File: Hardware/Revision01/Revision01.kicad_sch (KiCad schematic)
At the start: 21 parts, among them J1 Battery connector, SW1 Power-switch connection

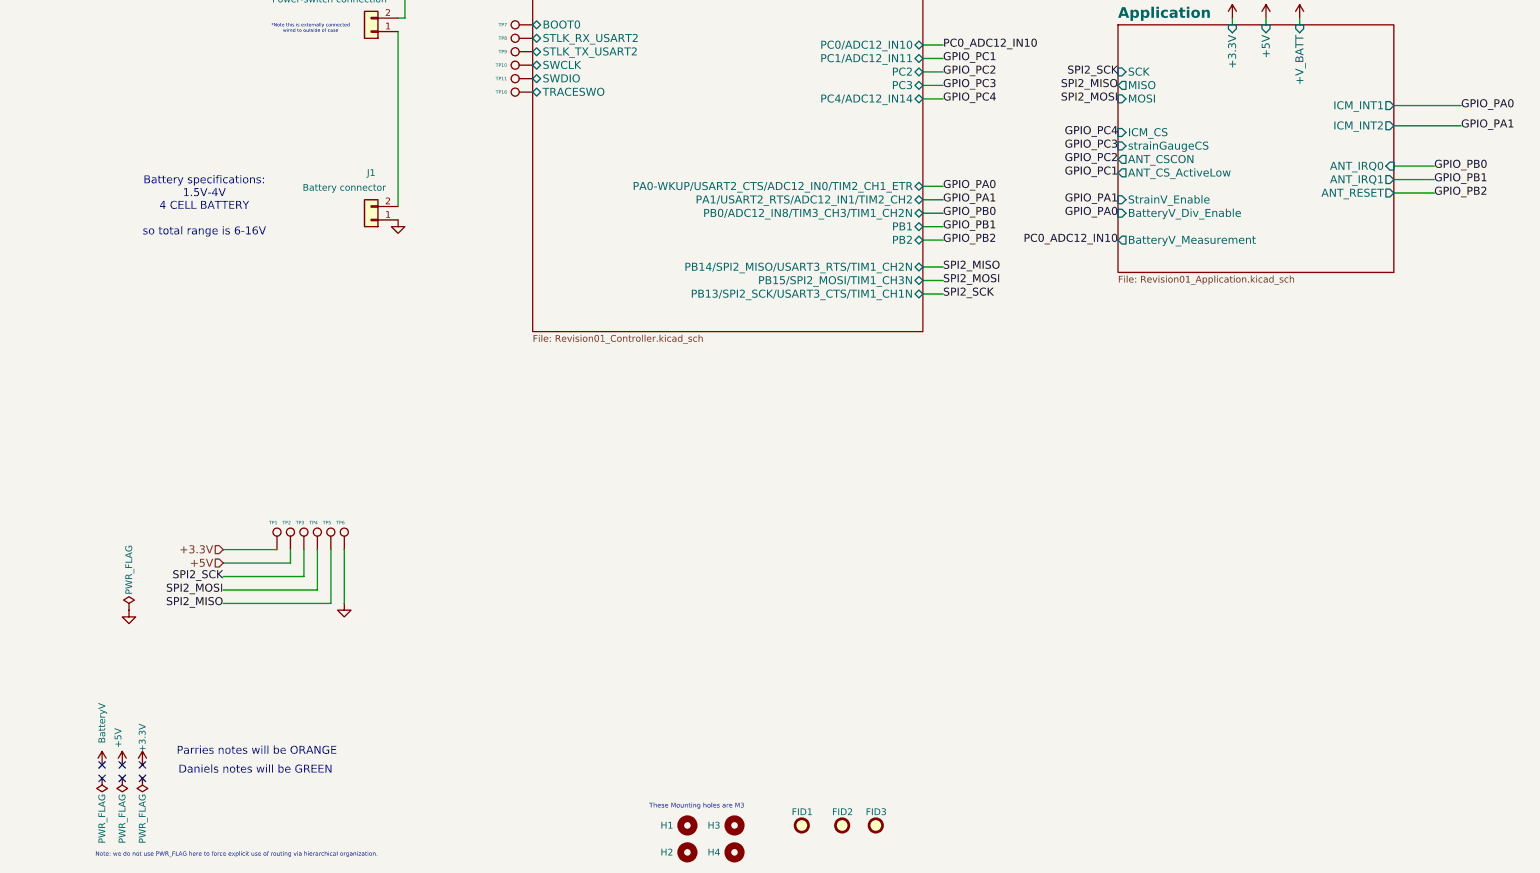
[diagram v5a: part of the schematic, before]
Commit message: made some progress on ERC
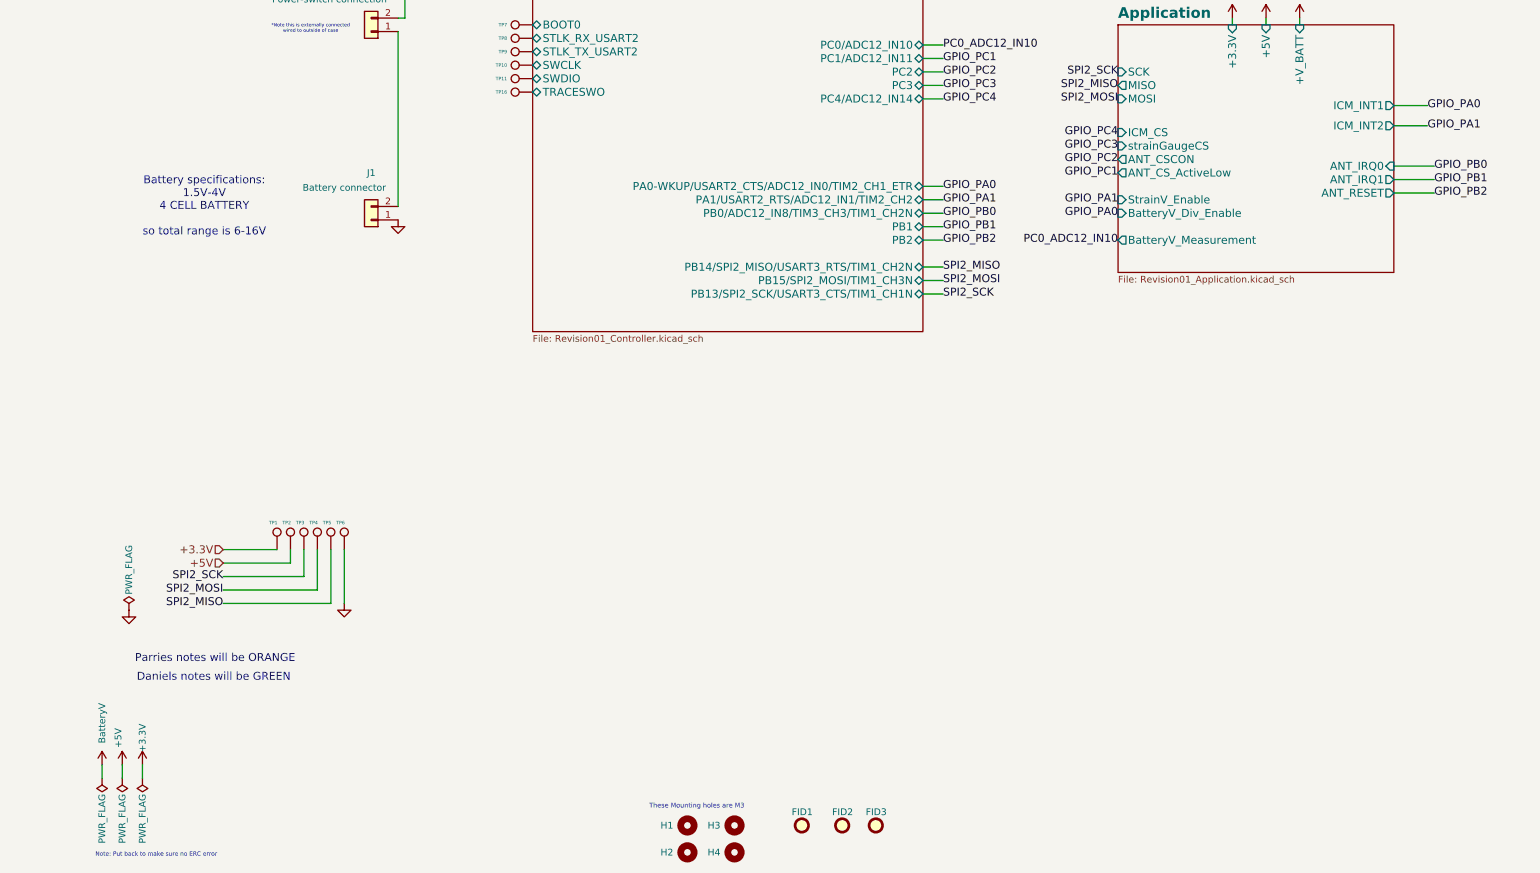
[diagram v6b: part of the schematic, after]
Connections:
- no-connect marks 6 -> 0
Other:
- note added: "Note: Put back to make sure no ERC error"
- note removed: "Note: we do not use PWR_FLAG here to force explicit use of routing via hierarchical organization."
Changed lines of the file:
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@@
 	(text "Daniels notes will be GREEN"
 		(exclude_from_sim no)
-		(at 50.546 178.816 0)
+		(at 42.672 161.29 0)
 		(effects
 			(font
@@
 	(text "Parries notes will be ORANGE"
 		(exclude_from_sim no)
-		(at 50.8 175.26 0)
+		(at 42.926 157.734 0)
 		(effects
 			(font
@@
 		)
 	)
-	(text "Note: we do not use PWR_FLAG here to force explicit use of routing via hierarchical organization."
+	(text "Note: Put back to make sure no ERC error"
 		(exclude_from_sim no)
 		(at 20.32 194.818 0)
@@
 		(color 0 0 0 0)
 	)
-	(no_connect
-		(at 29.21 180.34)
-	)
-	(no_connect
-		(at 29.21 177.8)
-	)
-	(no_connect
-		(at 21.59 180.34)
-	)
-	(no_connect
-		(at 21.59 177.8)
-	)
-	(no_connect
-		(at 25.4 180.34)
-	)
-	(no_connect
-		(at 25.4 177.8)
-	)
 	(wire
 		(pts
@@
 	(wire
 		(pts
+			(xy 29.21 177.8) (xy 29.21 180.34)
+		)
+		(stroke
+			(width 0)
+			(type default)
+		)
+	)
+	(wire
+		(pts
 			(xy 265.43 69.85) (xy 273.05 69.85)
 		)
@@
 	(wire
 		(pts
+			(xy 25.4 177.8) (xy 25.4 180.34)
+		)
+		(stroke
+			(width 0)
+			(type default)
+		)
+	)
+	(wire
+		(pts
 			(xy 64.77 147.32) (xy 64.77 137.16)
 		)
@@
 	(wire
 		(pts
-			(xy 265.43 53.34) (xy 278.13 53.34)
+			(xy 265.43 53.34) (xy 271.78 53.34)
 		)
 		(stroke
@@
 	(wire
 		(pts
+			(xy 21.59 177.8) (xy 21.59 180.34)
+		)
+		(stroke
+			(width 0)
+			(type default)
+		)
+	)
+	(wire
+		(pts
 			(xy 234.95 36.83) (xy 234.95 38.1)
 		)
@@
 	(wire
 		(pts
-			(xy 265.43 57.15) (xy 278.13 57.15)
+			(xy 265.43 57.15) (xy 271.78 57.15)
 		)
 		(stroke
@@
 	)
 	(label "GPIO_PA0"
-		(at 278.13 53.34 0)
+		(at 271.78 53.34 0)
 		(effects
 			(font
@@
 	)
 	(label "GPIO_PA1"
-		(at 278.13 57.15 0)
-		(effects
-			(font
+		(at 271.78 57.15 0)
+		(effects
+			(font

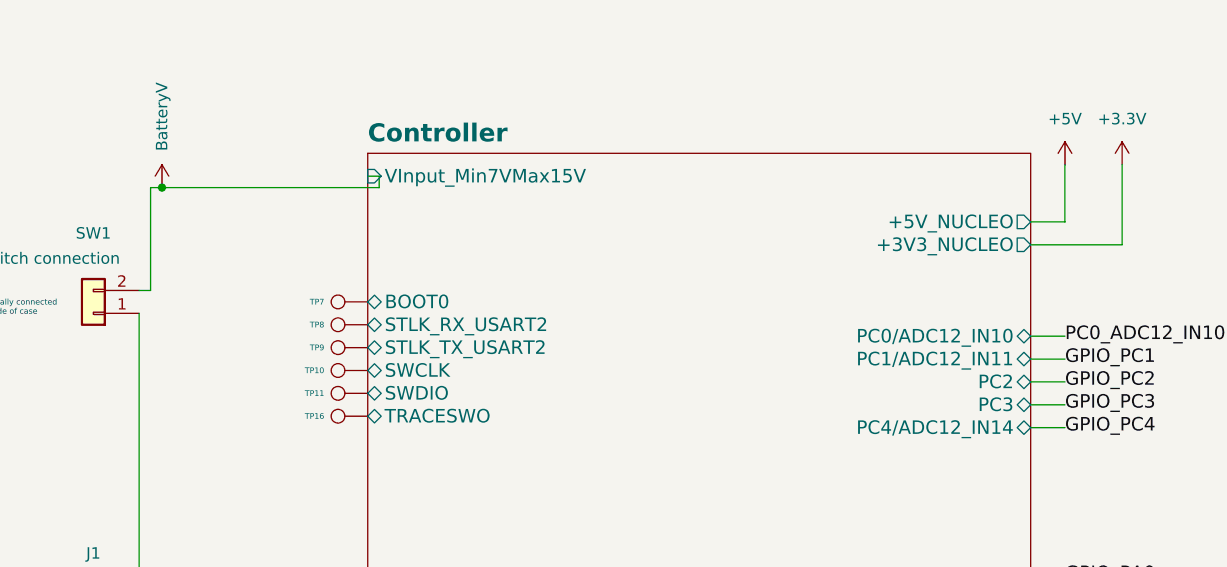
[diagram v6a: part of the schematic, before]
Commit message: Added new LDO to fit into battery range that feeds into MCU, make sure to remove power jumper wire before connecting. Completed ERC check
Still have to put on footprints for some components when doing PCB layout
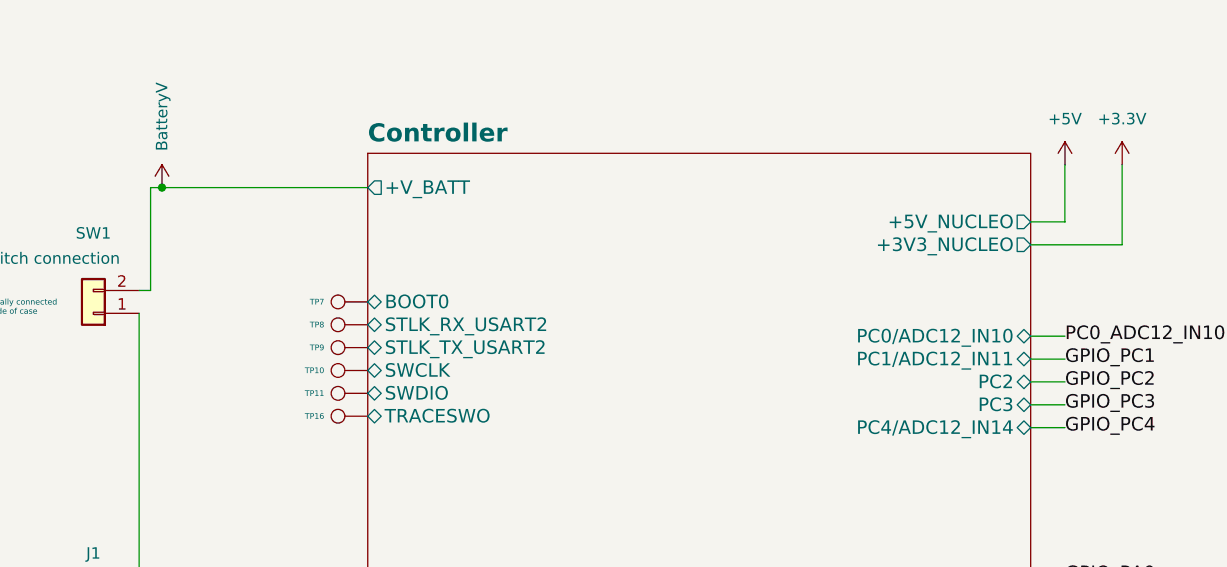
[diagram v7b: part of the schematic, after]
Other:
- sheet Controller ports: added +V_BATT; removed VInput_Min7VMax15V
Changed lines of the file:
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@@
 	(wire
 		(pts
-			(xy 180.34 49.53) (xy 176.53 49.53)
+			(xy 176.53 49.53) (xy 180.34 49.53)
 		)
 		(stroke
@@
 	(wire
 		(pts
-			(xy 104.14 24.13) (xy 102.87 24.13)
+			(xy 80.01 25.4) (xy 102.87 25.4)
 		)
 		(stroke
@@
 	(wire
 		(pts
-			(xy 104.14 24.13) (xy 104.14 25.4)
-		)
-		(stroke
-			(width 0)
-			(type default)
-		)
-	)
-	(wire
-		(pts
 			(xy 44.45 139.7) (xy 57.15 139.7)
 		)
@@
 	(wire
 		(pts
-			(xy 104.14 25.4) (xy 80.01 25.4)
-		)
-		(stroke
-			(width 0)
-			(type default)
-		)
-	)
-	(wire
-		(pts
 			(xy 59.69 137.16) (xy 59.69 142.24)
 		)
@@
 			)
 		)
-		(pin "VInput_Min7VMax15V" input
-			(at 102.87 24.13 180)
-			(effects
-				(font
-					(size 1.4986 1.4986)
-				)
-				(justify left)
-			)
-		)
 		(pin "+5V_NUCLEO" output
 			(at 176.53 29.21 0)
@@
 			(effects
 				(font
+					(size 1.4986 1.4986)
+				)
+				(justify left)
+			)
+		)
+		(pin "+V_BATT" output
+			(at 102.87 25.4 180)
+			(effects
+				(font

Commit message: todays review session
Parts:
- added BT1, BT2, BT3, BT4: Battery, symbol Device:Battery
- added SW2: SW_SPST_LED, symbol Switch:SW_SPST_LED
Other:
- note added: "+V_BATT is not an output"
- note added: "Add this case switch & LED to BOM"
- note added: "NEEDS TO FOLLOW PIN-Purpose Standard"
- note added: "NEEDS TO FOLLOW PIN_Purpose Standard"
- note added: "We need a battery symbol"
